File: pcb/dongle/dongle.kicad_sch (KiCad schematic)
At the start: 19 parts, among them U1 SeeeduinoXIAO

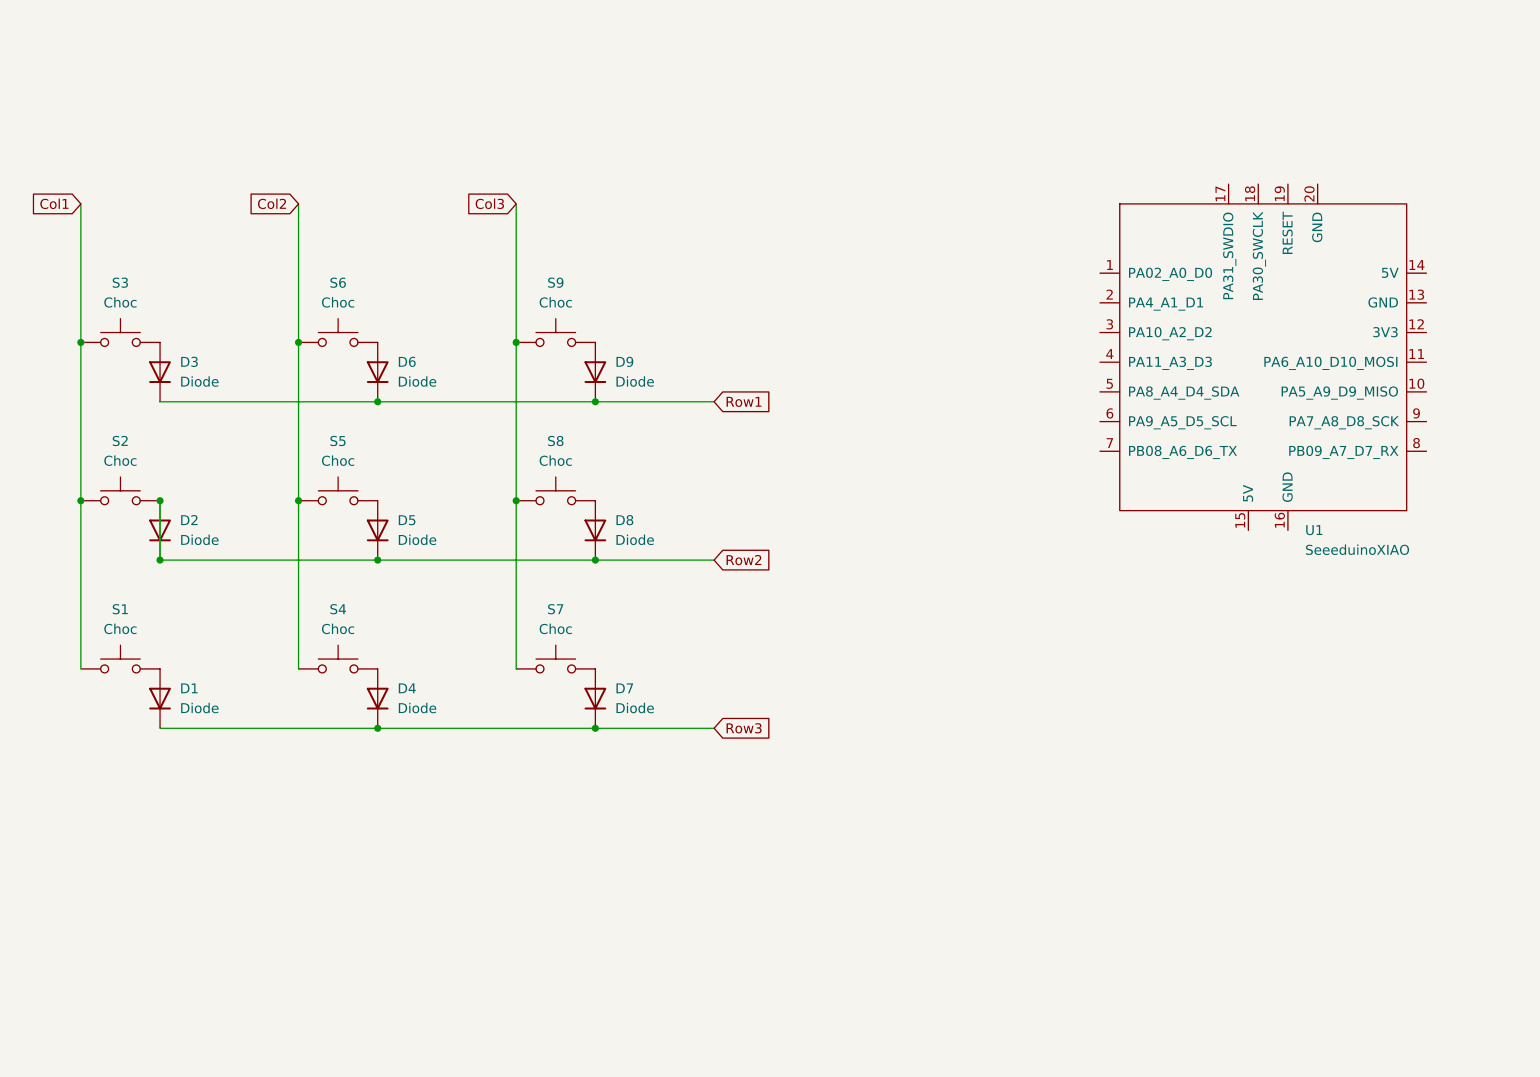
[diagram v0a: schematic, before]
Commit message: Added Dongle PCB and 3d"
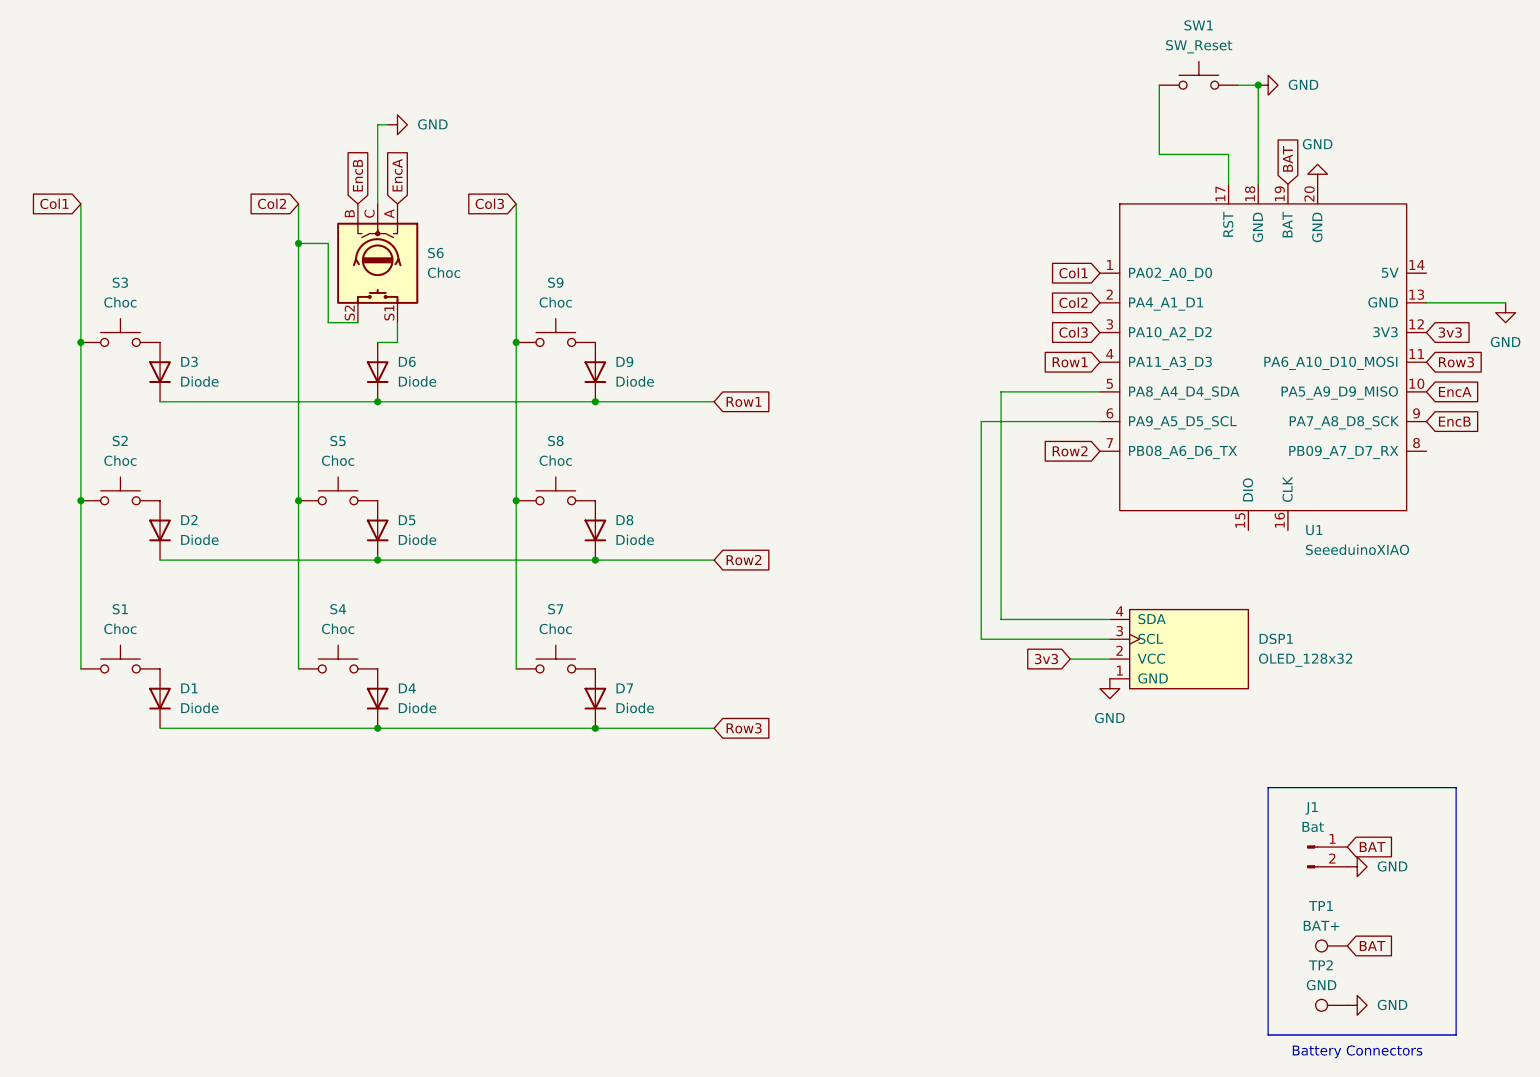
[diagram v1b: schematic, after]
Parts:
- added DSP1: OLED_128x32, ScottoKeebs_Components:OLED_128x32, symbol ScottoKeebs:OLED_128x32
- added J1: Bat, Connector_JST:JST_PH_S2B-PH-K_1x02_P2.00mm_Horizontal, symbol Connector:Conn_01x02_Pin
- added SW1: SW_Reset, Button_Switch_SMD:SW_SPST_EVQP7A, symbol Switch:SW_Push
- added TP1: BAT+, TestPoint:TestPoint_Pad_1.5x1.5mm, symbol Connector:TestPoint
- added TP2: GND, TestPoint:TestPoint_Pad_1.5x1.5mm, symbol Connector:TestPoint
- D1, D2, D3, D4, D5, D6, D7, D8, D9: symbol ScottoKeebs:Placeholder_Diode -> Device:D; LCSC PartNumber (none) -> C493190; MPN (none) -> C493190
- S1, S2, S3, S4, S5, S7, S8, S9: footprint Daprice_kbd_switches:Kailh_socket_PG1350 -> keyswitches:Kailh_socket_PG1350; LCSC PartNumber (none) -> C5333465; MPN (none) -> C5333465
- S6: footprint Daprice_kbd_switches:Kailh_socket_PG1350 -> Rotary_Encoder:RotaryEncoder_Alps_EC11E-Switch_Vertical_H20mm; symbol Switch:SW_Push -> Device:RotaryEncoder_Switch; Category (none) -> Sensors, Transducers; DK_Datasheet_Link (none) -> https://www.bourns.com/docs/Product-Datasheets/PEC11R.pdf; DK_Detail_Page (none) -> /product-detail/en/bourns-inc/PEC11R-4215F-S0024/PEC11R-421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; Digi-Key_PN (none) -> PEC11R-4215F-S0024-ND; Family (none) -> Encoders; Manufacturer (none) -> Bourns Inc.; Status (none) -> Active
- U1: footprint CF_Ergogen:Seeeduino XIAO-MOUDLE14P-2.54-21X17.8MM -> keeb_mcu:xiao-ble-smd-cutout
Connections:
- net Col1: now also U1.1 (PA02_A0_D0)
- net Col2: now also S6.S2, U1.2 (PA4_A1_D1); no longer S6.1
- net Col3: now also U1.3 (PA10_A2_D2)
- net Row1: now also U1.4 (PA11_A3_D3)
- net Row2: now also U1.7 (PB08_A6_D6_TX); no longer D2.2 (A), S2.2
- net Row3: now also U1.11 (PA6_A10_D10_MOSI)
- net at D6.2 (A): now also S6.S1; no longer S6.2
- net EncA: now reaches U1.10 (PA5_A9_D9_MISO)
- net EncA: now also S6.A
- net 3v3: now reaches U1.12 (3V3)
- net 3v3: now also DSP1.2 (VCC)
- net GND: now reaches U1.13 (GND)
- net GND: now also S6.C, U1.18 (GND), U1.20 (GND), DSP1.1 (GND), J1.2 (Pin_2), SW1.2, TP2.1
- net at U1.17 (RST): now also SW1.1
- net BAT: now reaches U1.19 (BAT)
- net BAT: now also J1.1 (Pin_1), TP1.1
- net at U1.5 (PA8_A4_D4_SDA): now also DSP1.4 (SDA)
- net at U1.6 (PA9_A5_D5_SCL): now also DSP1.3 (SCL)
- net EncB: now reaches U1.9 (PA7_A8_D8_SCK)
- net EncB: now also S6.B
- new net: D2.2 (A), S2.2
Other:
- note added: "Battery Connectors"
